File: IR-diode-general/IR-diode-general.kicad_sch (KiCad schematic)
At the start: 24 parts, among them J1 PJ-102A, J2 USB4105-GF-A, U1 MP2483DQ-LF-P, U2 AZ1117CH-5.0TRG1

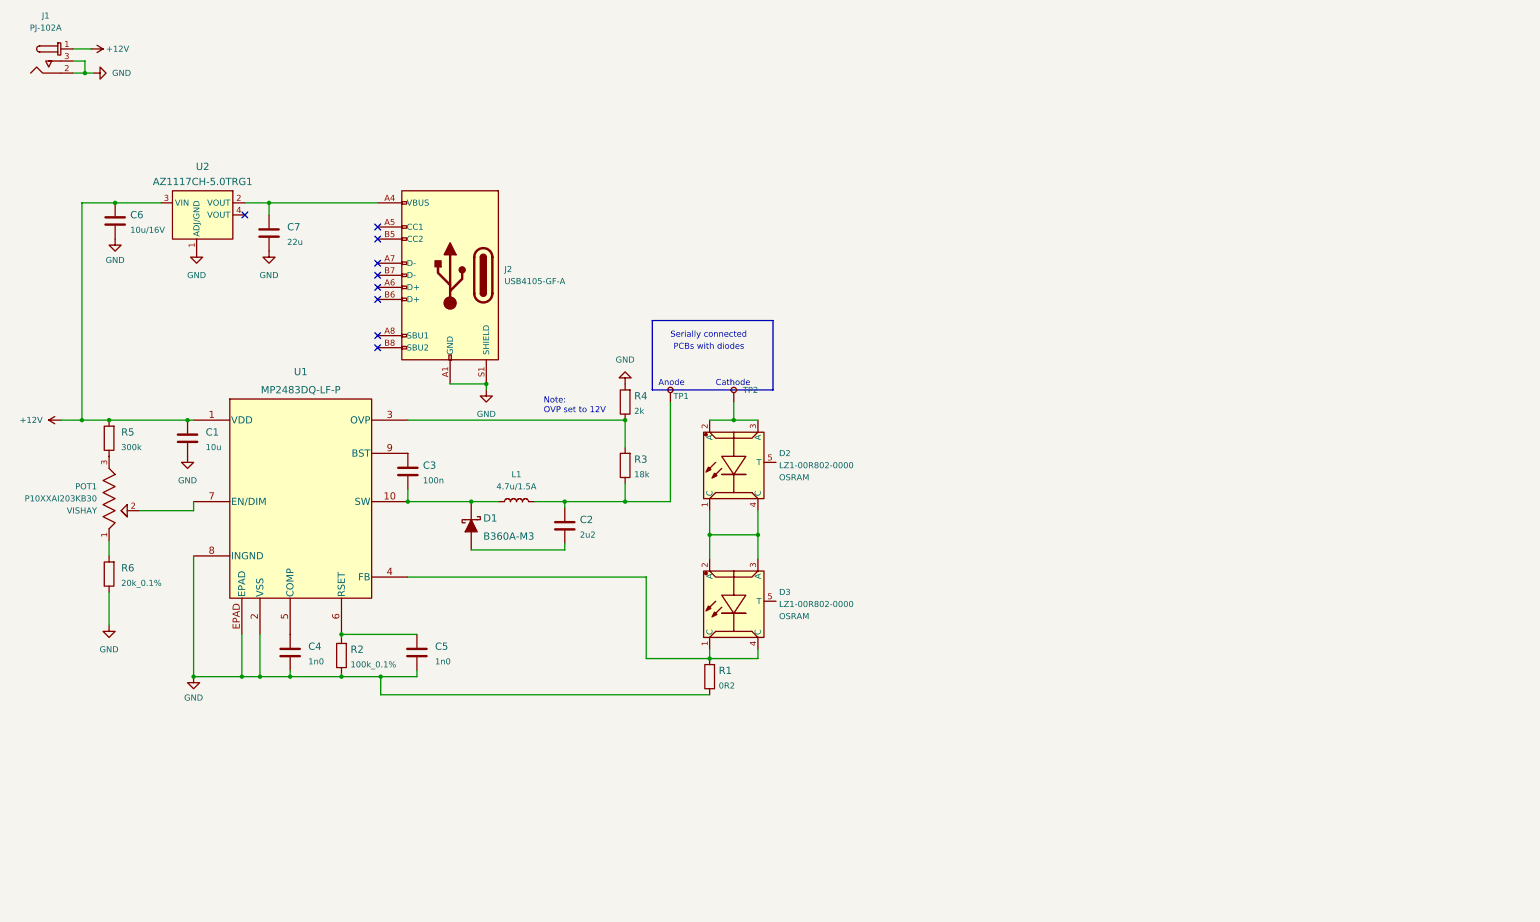
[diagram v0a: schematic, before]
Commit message: Rearranged project structure
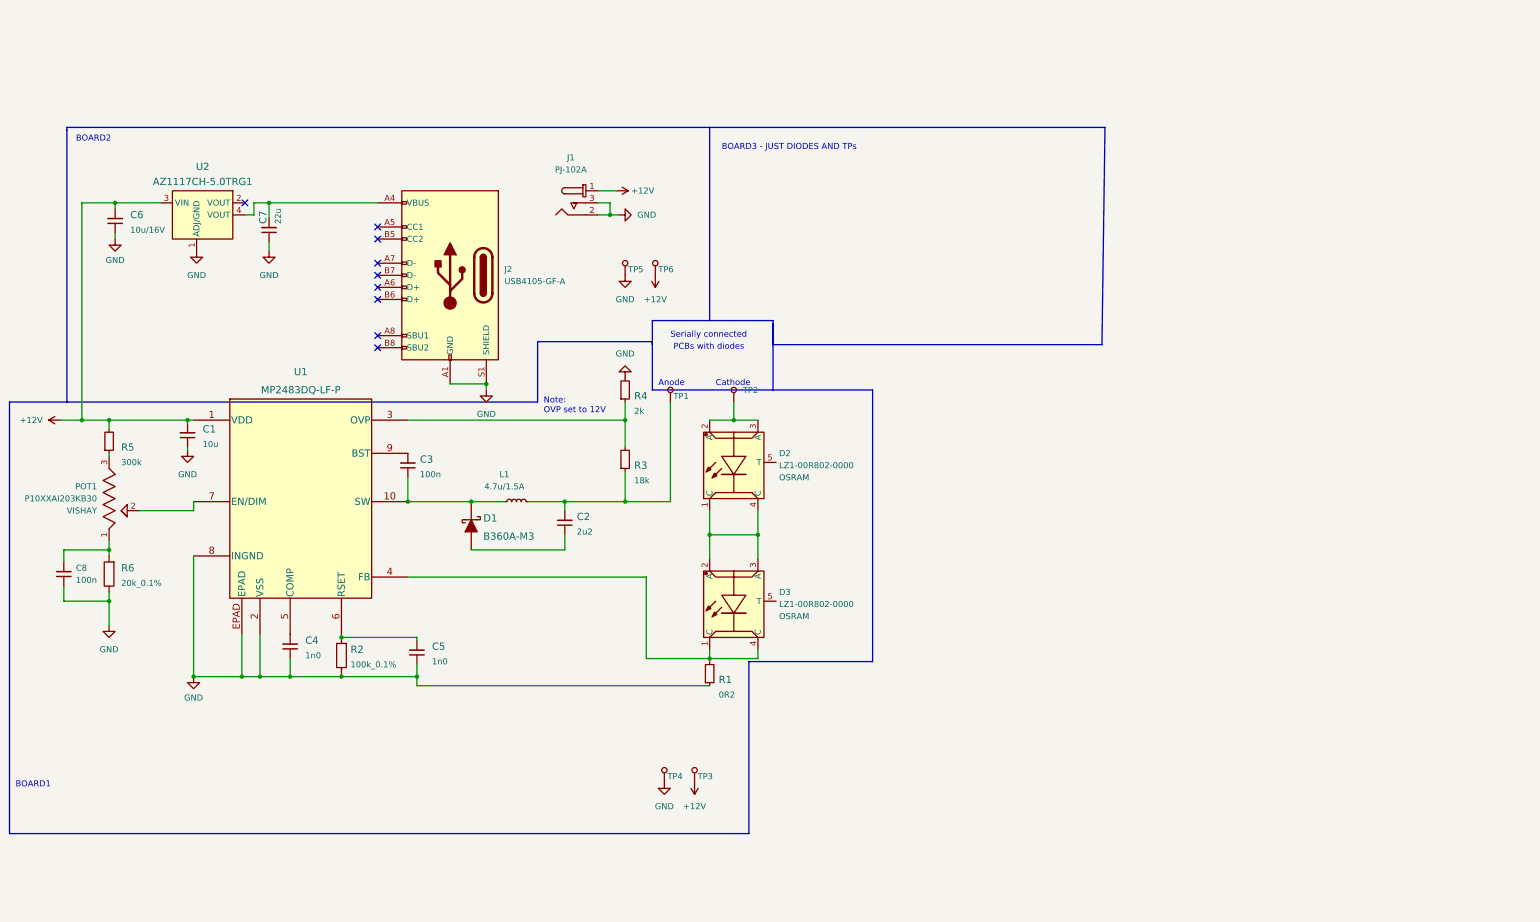
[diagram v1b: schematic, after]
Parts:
- added C8: C_100n_0402, antmicro-footprints:C_0402_1005Metric, symbol antmicroCapacitors0402:C_100n_0402
- added TP3, TP4, TP5, TP6: 5017, antmicro-footprints:PC_TEST-POINT_MINI_3.43x1.78mm, symbol antmicroTestPoints:5017
- C1, C4, C5, C6, L1: Copyright (none) -> Copyright (c) 2023 Antmicro; License (none) -> Apache-2.0 License
- C2, C7: footprint antmicro-footprints:0402-cap -> antmicro-footprints:C_0402_1005Metric; Copyright (none) -> Copyright (c) 2023 Antmicro; License (none) -> Apache-2.0 License
- C3: footprint antmicro-footprints:0402-cap -> antmicro-footprints:C_0402_1005Metric; Copyright (none) -> Copyright (c) 2023 Antmicro; Dielectric (none) -> X5R; License (none) -> Apache-2.0 License; Voltage (none) -> 50V
- R1: Copyright (none) -> Copyright (c) 2023 Antmicro; License (none) -> Apache-2.0 License; MPN ERJ-8BSFR20V -> CR1206-FX-0R20ELF; Manufacturer Panasonic -> Bourns; Tolerance (none) -> 1%
- R3: Copyright (none) -> Copyright (c) 2023 Antmicro; License (none) -> Apache-2.0 License; MPN MCWR04X1802FTL -> CR0402-FX-1802GLF; Manufacturer MULTICOMP -> Bourns; Tolerance (none) -> 1%
- R4: footprint antmicro-footprints:0402-res -> antmicro-footprints:R_0402_1005Metric; Copyright (none) -> Copyright (c) 2023 Antmicro; License (none) -> Apache-2.0 License; MPN CRCW04022K00FKED -> CR0402-FX-2001GLF; Manufacturer VISHAY -> Bourns; Tolerance (none) -> 1%
- R5: Copyright (none) -> Copyright (c) 2023 Antmicro; License (none) -> Apache-2.0 License; MPN CRCW0603300KFEA -> CR0603-FX-3003ELF; Manufacturer VISHAY -> Bourns; Tolerance (none) -> 1%
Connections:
- net +12V: now also C1.2, C6.2, TP3.1, TP6.1; no longer C1.1, C6.1
- net GND: now also C1.1, C4.1, C5.1, C6.1, C7.1, C8.1, TP4.1, TP5.1; no longer C1.2, C4.2, C5.2, C6.2, C7.2
- net at POT1.1, R6.2: now also C8.2
- net at L1.2, R3.1, TP1.1: now also C2.2; no longer C2.1
- net at D1.A: now also C2.1; no longer C2.2
- net at U1.5 (COMP): now also C4.2; no longer C4.1
- net at R2.2, U1.6 (RSET): now also C5.2; no longer C5.1
- net at D1.K, L1.1, U1.10 (SW): now also C3.1; no longer C3.2
- net at U1.9 (BST): now also C3.2; no longer C3.1
- net at J2.A4 (VBUS), J2.A9 (VBUS), J2.B4 (VBUS)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: now also C7.2, U2.4 (VOUT); no longer C7.1, U2.2 (VOUT)
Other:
- note added: "BOARD1"
- note added: "BOARD2"
- note added: "BOARD3 - JUST DIODES AND TPs"
- moved on the sheet: C1, C2, C3, C4, C5, C6, C7, R1, R3, R4, R5

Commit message: Add preliminary layout
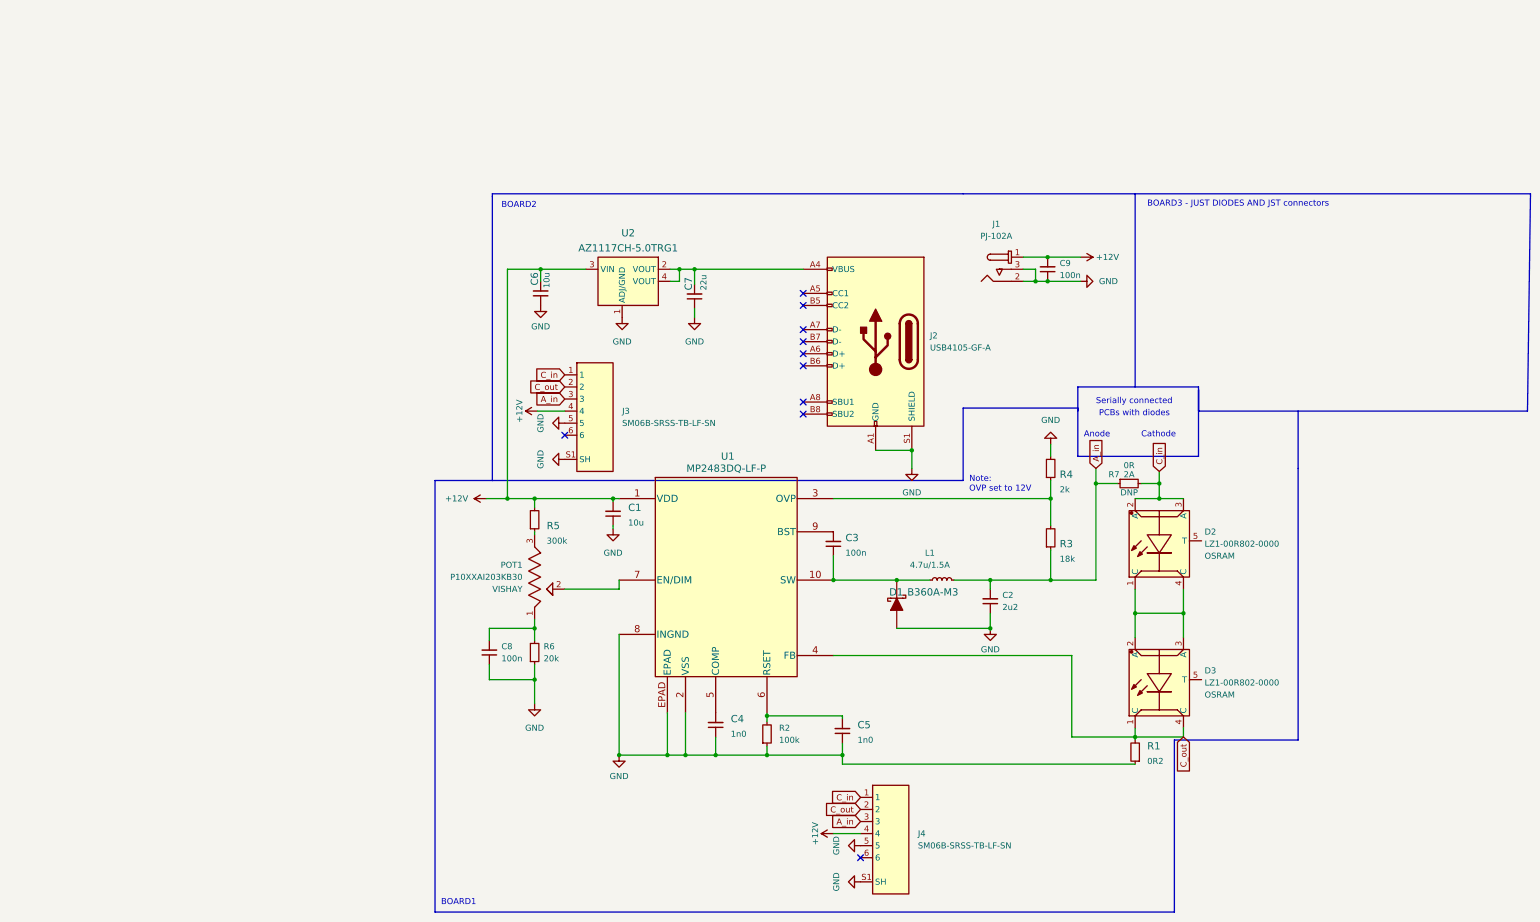
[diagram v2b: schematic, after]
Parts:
- removed C2: C_2u2_0402, antmicro-footprints:C_0402_1005Metric, symbol antmicroCapacitors0402:C_2u2_0402
- removed C6: C_10u_16V_0603, antmicro-footprints:0603-cap, symbol antmicroCapacitors0603:C_10u_16V_0603
- removed R2: R_100k_0.1%_0402, antmicro-footprints:0402-res, symbol antmicroResistors0402:R_100k_0.1%_0402
- removed R6: R_20k_0.1%_0402, antmicro-footprints:0402-res, symbol antmicroResistors0402:R_20k_0.1%_0402
- removed TP1, TP2, TP3, TP4, TP5, TP6: 5017, antmicro-footprints:PC_TEST-POINT_MINI_3.43x1.78mm, symbol antmicroTestPoints:5017
- added C2: C_2u2_0603, antmicro-footprints:0603-cap, symbol antmicroCapacitors0603:C_2u2_0603
- added C6: C_10u_0805, antmicro-footprints:0805-cap, symbol antmicroCapacitorsmisc:C_10u_0805
- added C9: C_100n_0402, antmicro-footprints:C_0402_1005Metric, symbol antmicroCapacitors0402:C_100n_0402
- added J3, J4: SM06B-SRSS-TB-LF-SN, antmicro-footprints:JST_SM06B-SRSS-TB-LF-SN, symbol antmicroRectangularConnectorsHeadersMalePins:SM06B-SRSS-TB-LF-SN
- added R2: R_100k_0402, antmicro-footprints:R_0402_1005Metric, symbol antmicroResistors0402:R_100k_0402
- added R6: R_20k_0402, antmicro-footprints:R_0402_1005Metric, symbol antmicroResistors0402:R_20k_0402
- added R7: R_0R_1206, antmicro-footprints:R_1206_3216Metric, symbol antmicroResistorsmisc:R_0R_1206
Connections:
- net +12V: now also C6.2, C9.2, J3.4, J4.4
- net GND: now also D1.1 (A), C2.1, C6.1, C9.1, J3.5, J3.S1 (SH), J3.S2 (SH), J4.5, J4.S1 (SH), J4.S2 (SH), R2.1, R6.1
- net at C8.2, POT1.1: now also R6.2
- net A_in: now reaches L1.2, R3.1
- net A_in: now also C2.2, J3.3, J4.3, R7.1
- net at C5.2, U1.6 (RSET): now also R2.2
- net at C3.1, L1.1, U1.10 (SW): now also D1.2 (K); no longer D1.K
- net C_out: now reaches D3.1 (C), D3.4 (C), R1.2, U1.4 (FB)
- net C_out: now also J3.2, J4.2
- net C_in: now reaches D2.2 (A), D2.3 (A)
- net C_in: now also J3.1, J4.1, R7.2
- net at U2.2 (VOUT): now also C7.2, J2.A4 (VBUS), J2.A9 (VBUS), J2.B4 (VBUS), J2.B9 (VBUS), U2.4 (VOUT)
- no-connect marks 9 -> 10
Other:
- note added: "BOARD3 - JUST DIODES AND JST connectors"
- note removed: "BOARD3 - JUST DIODES AND TPs"
- moved on the sheet: C1, C3, C4, C5, C7, C8, D1, D2, D3, J1, J2, L1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
